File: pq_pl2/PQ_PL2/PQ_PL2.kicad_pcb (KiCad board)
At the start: 2 copper layers, 40 x 40 mm, 66 parts, among them J1 SLW-110-01-T-S, J2 SLW-110-01-T-S, J3 SLW-110-01-T-S, J4 SLW-110-01-T-S

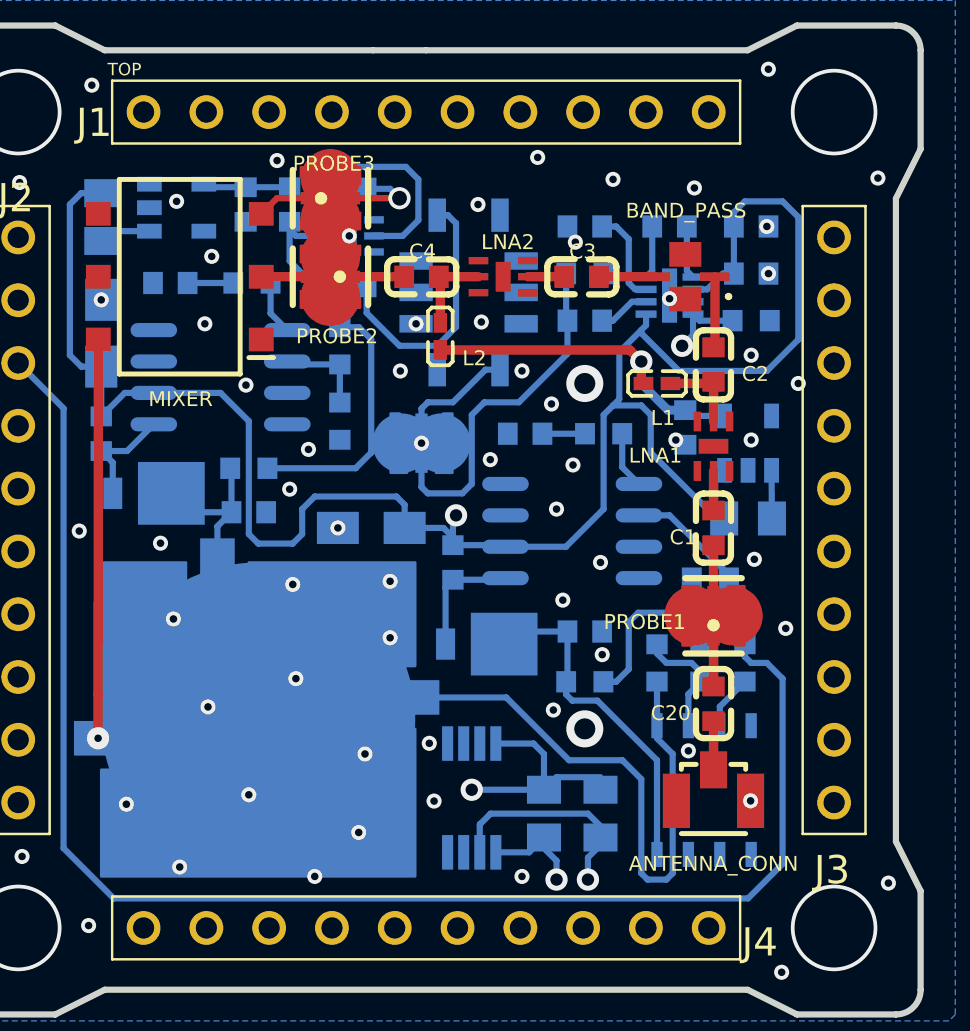
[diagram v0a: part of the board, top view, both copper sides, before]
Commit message: Solved old design components&library altium import problems. Pre KiCad7
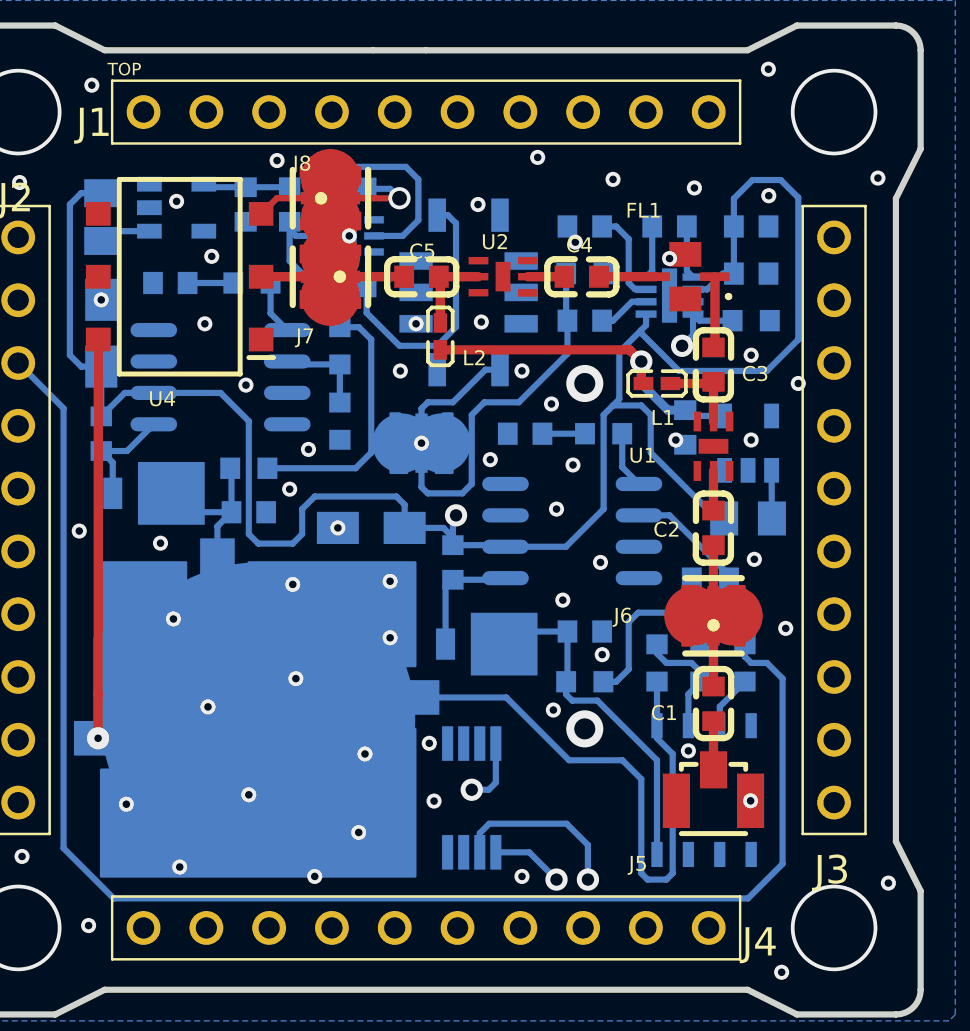
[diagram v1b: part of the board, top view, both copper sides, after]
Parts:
- removed R13, R14: 5k, easyeda:R0805
- renumbered C20 to C1, C13 to C10, C14 to C11, C15 to C12, C11 to C13, C7 to C14, C9 to C15, C12 to C16, C8 to C17, C10 to C18, C1 to C2, C18 to C20, C2 to C3, C3 to C4, C4 to C5, C5 to C6, C6 to C7, C17 to C8, C16 to C9, BAND_PASS to FL1, SAW to FL2, VCO to G1, ANTENNA_CONN to J5, PROBE1 to J6, PROBE2 to J7, PROBE3 to J8, PROBE4 to J9, R8 to R1, R3 to R10, R4 to R11, R2 to R12, R9 to R2, R10 to R3, R12 to R4, R11 to R5, R5 to R6, R6 to R7, R7 to R8, R1 to R9, LNA1 to U1, B3.6VRF to U10, B3.6VIF to U11, TSENS to U12, LNA2 to U2, OPAMP to U3, MIXER to U4, LNA3 to U5, B10V to U8, B22V to U9
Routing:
- net (no net): track 559.7 -> 552.0 mm, vias 78 -> 77
- added copper zone on In1.Cu, net (none)
- added copper zone on In2.Cu, net (none)
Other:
- copper layers 2 -> 4

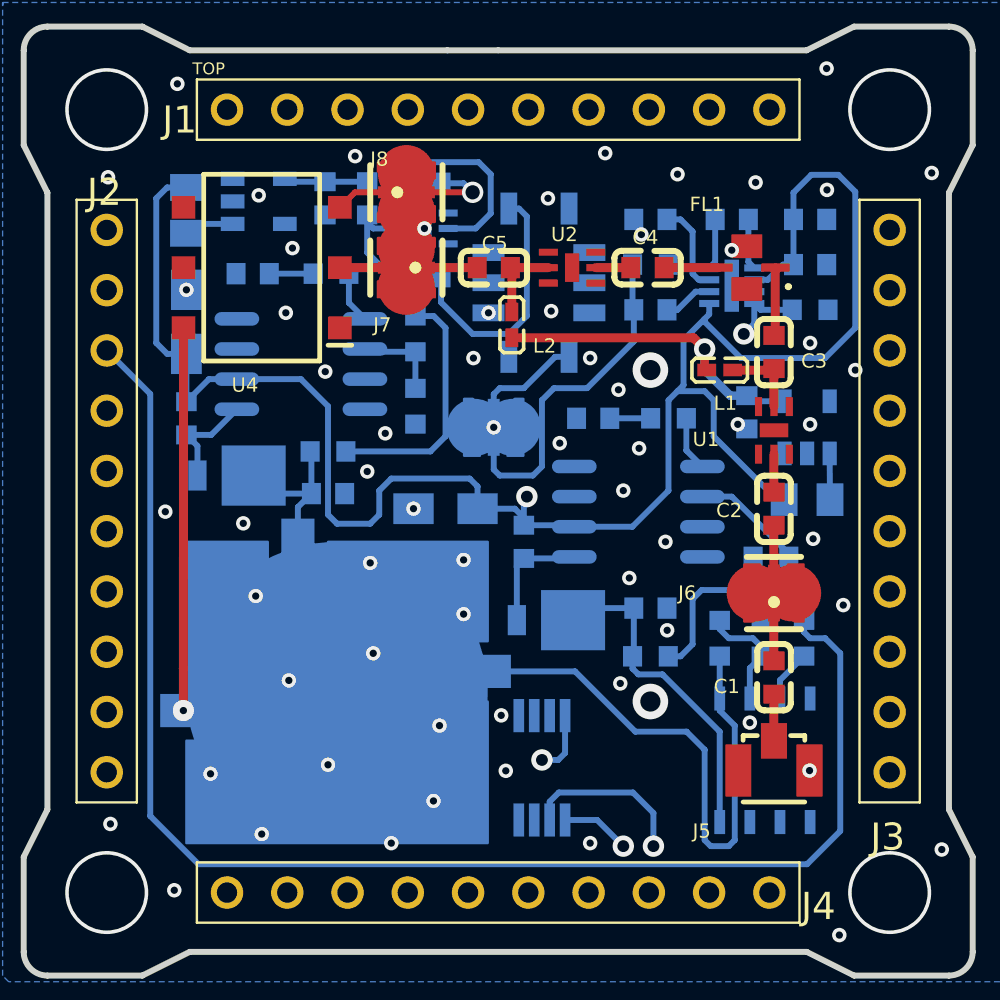
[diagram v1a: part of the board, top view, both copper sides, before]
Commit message: Full Kicad7 transition, library improvement and adaptation, correct footprints and 3D models added
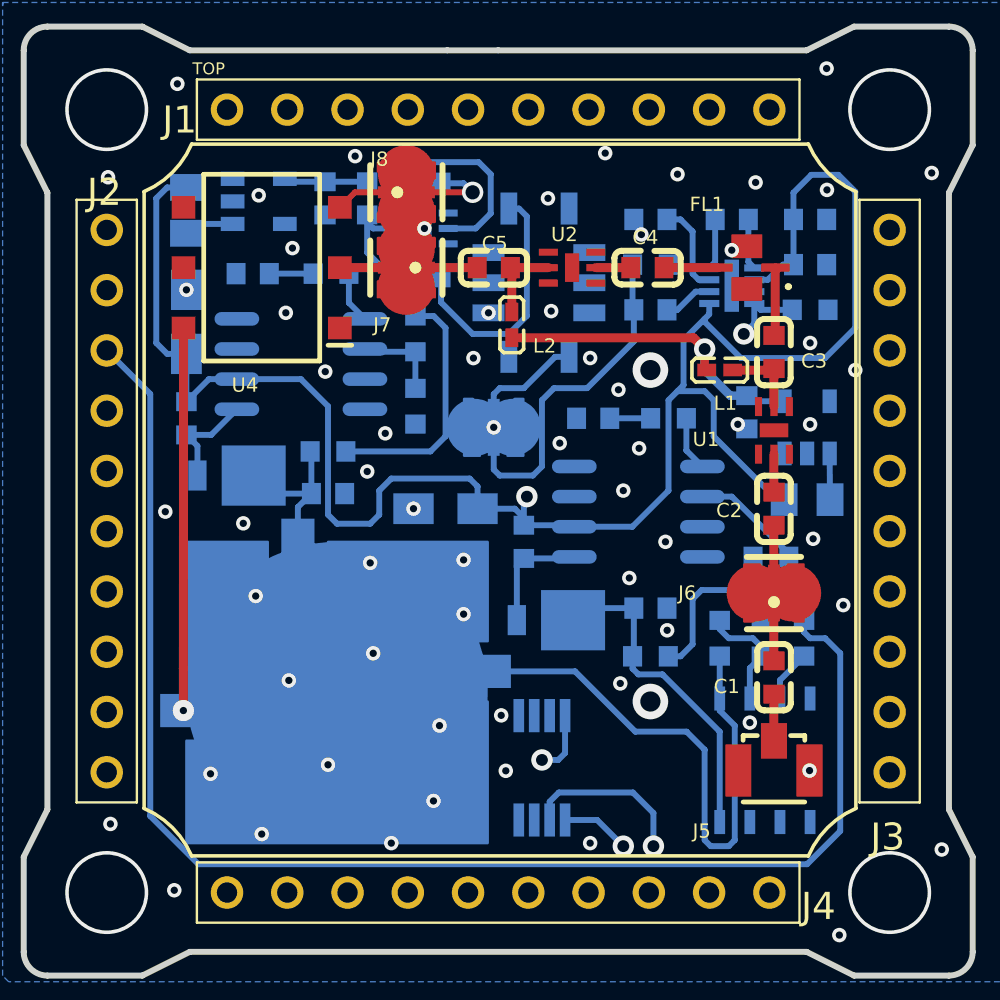
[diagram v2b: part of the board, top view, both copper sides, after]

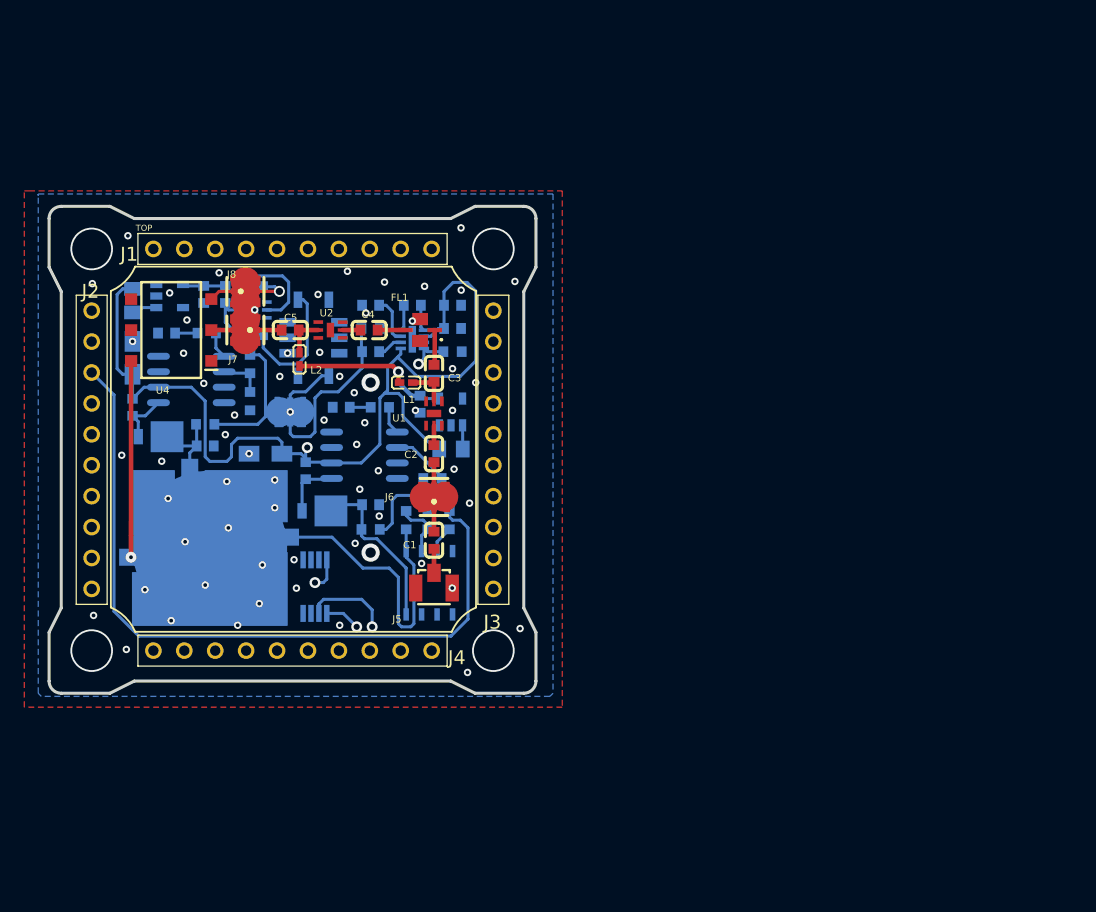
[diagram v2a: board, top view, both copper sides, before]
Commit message: P/L2 schematic revision and preliminary layout formulation: tranmission lines and block biasing
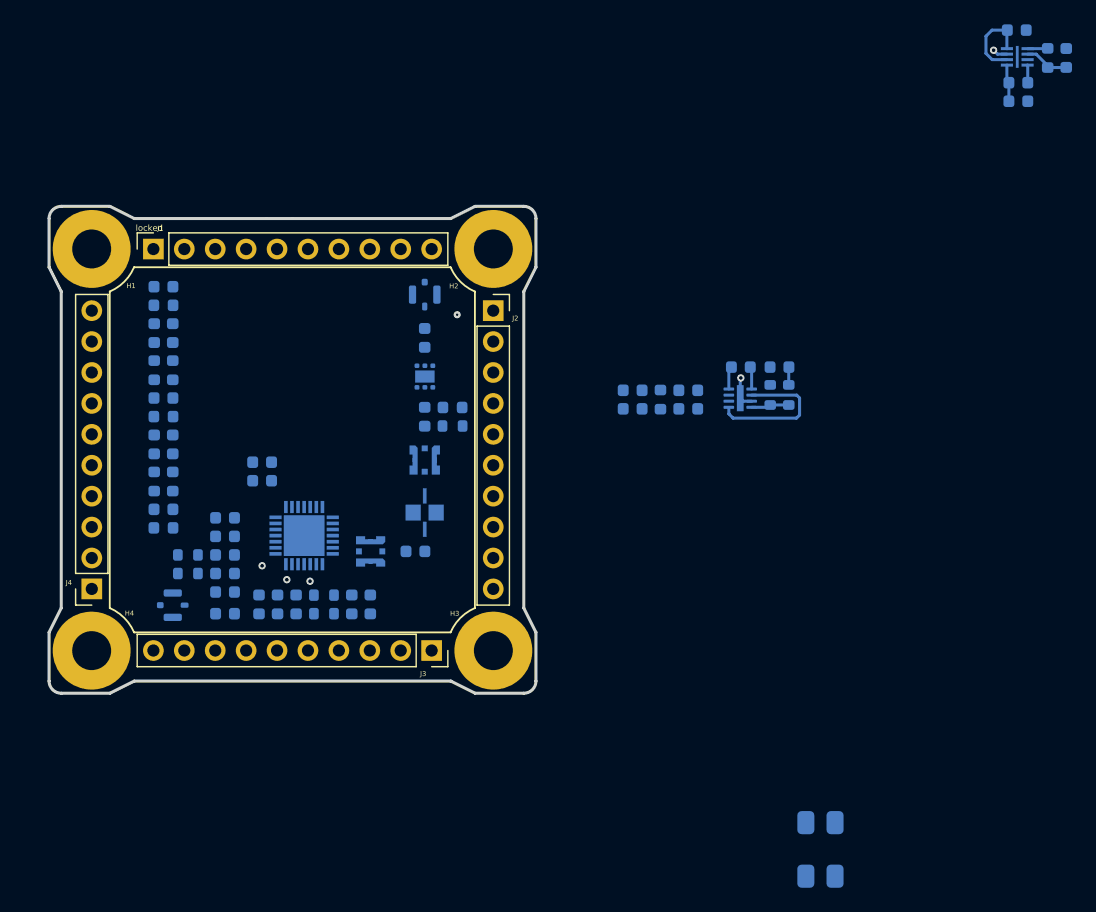
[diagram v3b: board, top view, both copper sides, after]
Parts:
- removed D1, D2: MBRM120ET3G, easyeda:POWERMITE_L2.0-W1.9-LS3.8-RD
- removed FL2: SF2242B, easyeda:SMP-03-10 5X7 MM
- removed G1: CVCO55CW, easyeda:CVCO55CW
- removed J9: MS-156C3, easyeda:IPEX-SMD_MS-156C3
- removed R10: 160K, easyeda:R0603
- removed R11: 10K, easyeda:R0603
- removed R12, R9: 68K, easyeda:R0603
- removed R8: 20K, easyeda:R0603
- removed RSSI: LT5537EDDB#TRMPBF, easyeda:SON50P200X300X80-9N
- removed U10, U11: TPS613226ADBVT, easyeda:SOT-23-5_L2.9-W1.6-P0.95-LS2.8-BR
- removed U12: TCN75AVUA713-VAO, easyeda:SOP65P490X110-8N
- removed U5: LEE2-6+, easyeda:SON65P200X200X105-7N
- removed U8, U9: LT1949ES8#PBF, easyeda:SO-8_L4.9-W3.9-P1.27-LS5.9-BL
- added Annotation1: Silkscreen_Annotation, -nsl_symbols:Bridgemaker, B.Cu at (166.8, 36.0)
- added Annotation2: Silkscreen_Annotation, -nsl_symbols:GRSS, B.Cu at (175.5, 30.8)
- added C21: 1.3pF, Capacitor_SMD:C_0603_1608Metric, B.Cu at (93.2, 58.7)
- added C22: 1.3pF, Capacitor_SMD:C_0603_1608Metric, B.Cu at (91.7, 58.7)
- added C23: 310pF, Capacitor_SMD:C_0603_1608Metric, B.Cu at (92.5, 64.0)
- added C24: 12 pF, Capacitor_SMD:C_0603_1608Metric, B.Cu at (131.0, 55.8)
- added C25: 12 pF, Capacitor_SMD:C_0603_1608Metric, B.Cu at (131.0, 54.2)
- added C26: 10nF, Capacitor_SMD:C_0603_1608Metric, B.Cu at (135.6, 55.8)
- added C27: 10nF, Capacitor_SMD:C_0603_1608Metric, B.Cu at (135.6, 54.2)
- added C28: 27pF, Capacitor_SMD:C_0603_1608Metric, B.Cu at (143.1, 52.3)
- added C29: 33nF, Capacitor_SMD:C_0603_1608Metric, B.Cu at (139.9, 52.3)
- added C30: 1uF, Capacitor_SMD:C_0603_1608Metric, B.Cu at (166.6, 26.9)
- added C31: 4.7uF, Capacitor_SMD:C_0603_1608Metric, B.Cu at (162.6, 24.6)
- added C32: 1nF, Capacitor_SMD:C_0603_1608Metric, B.Cu at (162.7, 29.0)
- added C33: 1uF, Capacitor_SMD:C_0603_1608Metric, B.Cu at (162.7, 30.5)
- added H1: MountingHole_Pad, MountingHole:MountingHole_3.2mm_M3_Pad, F.Cu at (86.6, 42.6)
- added H2: MountingHole_Pad, MountingHole:MountingHole_3.2mm_M3_Pad, F.Cu at (119.6, 42.6)
- added H3: MountingHole_Pad, MountingHole:MountingHole_3.2mm_M3_Pad, F.Cu at (119.6, 75.6)
- added H4: MountingHole_Pad, MountingHole:MountingHole_3.2mm_M3_Pad, F.Cu at (86.6, 75.6)
- added L10: 4.7uH, Inductor_SMD:L_0603_1608Metric, B.Cu at (165.1, 26.9)
- added L8: 16.4nH, Inductor_SMD:L_0603_1608Metric, B.Cu at (92.5, 65.5)
- added L9: 680 nH, Inductor_SMD:L_0603_1608Metric, B.Cu at (133.3, 55.0)
- added X1: 406C35B14M, -nsl_miscellaneous:406C35B14M, B.Cu at (146.4, 91.9)
- C1: value 33nF -> 1nF; footprint easyeda:C0603 -> Capacitor_SMD:C_0603_1608Metric; moved to B.Cu
- C10: value 1nF -> 47nF; footprint easyeda:C0603 -> Capacitor_SMD:C_0603_1608Metric; moved to B.Cu
- C11: value 1uF -> 82pF; footprint easyeda:C0603 -> Capacitor_SMD:C_0603_1608Metric; moved to B.Cu
- C12: value 33nF -> 10nF; footprint easyeda:C0603 -> Capacitor_SMD:C_0603_1608Metric; moved to B.Cu
- C13, C16: value 10uF -> 1.2nF; footprint easyeda:C0603 -> Capacitor_SMD:C_0603_1608Metric; moved to B.Cu
- C14: value 330pF -> 47nF; footprint easyeda:C0603 -> Capacitor_SMD:C_0603_1608Metric; moved to B.Cu
- C15: value 22u -> 1.2nF; footprint easyeda:CAPPM3216X180N -> Capacitor_SMD:C_0603_1608Metric; moved to B.Cu
- C17: value 330pF -> 310pF; footprint easyeda:C0603 -> Capacitor_SMD:C_0603_1608Metric; moved to B.Cu
- C18: value 22u -> 1.3pF; footprint easyeda:CAPPM3216X180N -> Capacitor_SMD:C_0603_1608Metric; moved to B.Cu
- C19: value 22uF -> 1.3pF; footprint easyeda:C0603 -> Capacitor_SMD:C_0603_1608Metric; moved to B.Cu
- C2, C3, C4: value 10pF -> 1nF; footprint easyeda:C0603 -> Capacitor_SMD:C_0603_1608Metric; moved to B.Cu
- C20: value 22uF -> 500pF; footprint easyeda:C0603 -> Capacitor_SMD:C_0603_1608Metric; moved to B.Cu
- C5: value 10pF -> 47nF; footprint easyeda:C0603 -> Capacitor_SMD:C_0603_1608Metric; moved to B.Cu
- C6, C7, C8, C9: value 100pF -> 47nF; footprint easyeda:C0603 -> Capacitor_SMD:C_0603_1608Metric; moved to B.Cu
- FL1: value BFCG-162W+ -> BFCG162W; footprint easyeda:BFCG162W -> -nsl_rf:GE0805C-3; moved to B.Cu
- J1, J2, J3, J4: footprint easyeda:SLW-110-01-X-S -> -nsl_connector:SLW-110-01
- J5: value U.FL-R-SMT-1(10) -> U.FL-R-SMT; footprint easyeda:ANT-SMD_UFL-R-SMT-1-10 -> -nsl_connector:C.FL-R-SMT-1(90); moved to B.Cu
- J6, J7: footprint easyeda:IPEX-SMD_MS-156C3 -> -nsl_connector:CoaxialSwitch_Hirose_MS-156C3_Horizontal; moved to B.Cu
- J8: value MS-156C3 -> U.FL-R-SMT; footprint easyeda:IPEX-SMD_MS-156C3 -> -nsl_connector:C.FL-R-SMT-1(90); moved to B.Cu
- L1: footprint easyeda:L0402 -> Inductor_SMD:L_0603_1608Metric; moved to B.Cu
- L2: value 100nH -> 16.4nH; footprint easyeda:L0402 -> Inductor_SMD:L_0603_1608Metric; moved to B.Cu
- L3: value 3.3uH -> 3.9nH; footprint easyeda:L0603 -> Inductor_SMD:L_0603_1608Metric; moved to B.Cu
- L4: value 10uH -> 3.9nH; footprint easyeda:L0603 -> Inductor_SMD:L_0603_1608Metric; moved to B.Cu
- L5: value 10uH -> 10.2nH; footprint easyeda:L0603 -> Inductor_SMD:L_0603_1608Metric; moved to B.Cu
- L6, L7: value 4.7uH -> 3.9nH; footprint easyeda:L0805 -> Inductor_SMD:L_0603_1608Metric; moved to B.Cu
- R1: value 10K -> 87.5; footprint easyeda:R0603 -> Resistor_SMD:R_0603_1608Metric; moved to B.Cu
- R2: value 20K -> 75; footprint easyeda:R0603 -> Resistor_SMD:R_0603_1608Metric; moved to B.Cu
- R3: value 100K -> 75; footprint easyeda:R0603 -> Resistor_SMD:R_0603_1608Metric; moved to B.Cu
- R4: value 51 -> 18k; footprint easyeda:R0603 -> Resistor_SMD:R_0603_1608Metric; moved to B.Cu
- R5: value 33K -> 2.2k; footprint easyeda:R0603 -> Resistor_SMD:R_0603_1608Metric; moved to B.Cu
- R6: value 120K -> 33K; footprint easyeda:R0603 -> Resistor_SMD:R_0603_1608Metric; moved to B.Cu
- R7: value 20K -> 33K; footprint easyeda:R0603 -> Resistor_SMD:R_0603_1608Metric; moved to B.Cu
- U1: footprint easyeda:SON65P200X200X105-7N -> Package_SON:WSON-6-1EP_2x2mm_P0.65mm_EP1x1.6mm; moved to B.Cu
- U2: value LEE2-6+ -> MAX2121; footprint easyeda:SON65P200X200X105-7N -> -nsl_rf:QFN50P500X500X80-29N; moved to B.Cu
- U3: value LM258WDT -> LT5537EDDB; footprint easyeda:SO8 -> Package_DFN_QFN:DFN-8-1EP_2x3mm_P0.5mm_EP0.56x2.15mm; moved to B.Cu
- U4: value ADE-11X+ -> LT3048; footprint easyeda:SOTFL254P691X284-6N -> -nsl_power:SON45P200X200X80-9N; moved to B.Cu
- moved U4 73.0 mm to (162.6, 26.8)
- moved R6 46.5 mm to (142.3, 54.6), turned to -90 degrees
- moved R7 44.3 mm to (143.8, 54.6)
- moved J2 33.0 mm to (119.6, 47.7), turned to 0 degrees
- moved U3 31.0 mm to (139.8, 54.9), turned to 0 degrees
- moved J3 28.4 mm to (114.5, 75.6)
- moved C14 27.9 mm to (109.5, 71.8), turned to -90 degrees
- moved C10 27.5 mm to (97.5, 69.3), turned to 0 degrees
- moved J8 26.5 mm to (93.2, 71.9), turned to -90 degrees
- moved C12 26.4 mm to (103.4, 71.8), turned to -90 degrees
- moved C4 26.1 mm to (97.5, 72.6)
- moved C11 25.9 mm to (107.9, 71.8), turned to -90 degrees
- moved L7 24.5 mm to (91.7, 61.7), turned to 90 degrees
- moved R5 24.0 mm to (105.6, 72.6), turned to 0 degrees
- moved C9 23.7 mm to (97.5, 67.8)
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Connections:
- C1 pad 1: (no net) -> Net-(C1-Pad1)
- C1 pad 2: (no net) -> Net-(U1-In)
- C10 pad 1: (no net) -> Net-(C10-Pad1)
- C10 pad 2: (no net) -> Net-(U2-QOUT+)
- C11 pad 1: (no net) -> Net-(U2-TUNEVCO)
- C11 pad 2: (no net) -> GND
- C12 pad 1: (no net) -> Net-(U2-CPOUT)
- C12 pad 2: (no net) -> Net-(C12-Pad2)
- C13 pad 1: (no net) -> Net-(U2-CPOUT)
- C13 pad 2: (no net) -> GND
- C14 pad 1: (no net) -> Net-(U2-BYPVCO)
- C14 pad 2: (no net) -> GND
- C15 pad 1: (no net) -> Net-(U2-XTAL)
- C15 pad 2: (no net) -> Net-(C15-Pad2)
- C16 pad 1: (no net) -> Net-(U2-REFOUT)
- C16 pad 2: (no net) -> Net-(C16-Pad2)
- C17 pad 1: (no net) -> IF-
- C17 pad 2: (no net) -> IF+
- C18 pad 1: (no net) -> Net-(C18-Pad1)
- C18 pad 2: (no net) -> IF+
- C19 pad 1: (no net) -> Net-(C19-Pad1)
- C19 pad 2: (no net) -> IF-
- C2 pad 1: (no net) -> Net-(U1-Out&DCin)
- C2 pad 2: (no net) -> Net-(C2-Pad2)
- C20 pad 1: (no net) -> Net-(C20-Pad1)
- C20 pad 2: (no net) -> Net-(C20-Pad2)
- C3 pad 1: (no net) -> Net-(FL1-Out)
- C3 pad 2: (no net) -> RF
- C4 pad 1: (no net) -> P/L_POWER
- C4 pad 2: (no net) -> GND
- C5 pad 1: (no net) -> Net-(U2-QDC+)
- C5 pad 2: (no net) -> Net-(U2-QDC-)
- C6 pad 1: (no net) -> Net-(U2-IDC+)
- C6 pad 2: (no net) -> Net-(U2-IDC-)
- C7 pad 1: (no net) -> IF-
- C7 pad 2: (no net) -> IO-
- C8 pad 1: (no net) -> IF+
- C8 pad 2: (no net) -> IO+
- C9 pad 1: (no net) -> Net-(C9-Pad1)
- C9 pad 2: (no net) -> Net-(U2-QOUT-)
- FL1 pad 1: (no net) -> Net-(FL1-IN)
- FL1 pad 2: (no net) -> GND
- FL1 pad 3: (no net) -> Net-(FL1-Out)
- FL1 pad 4: (no net) -> GND
- J1 pad 1: (no net) -> SDA1
- J1 pad 10: (no net) -> 3V3_PERM
- J1 pad 2: (no net) -> SCL1
- J1 pad 3: (no net) -> UART_RX
- J1 pad 4: (no net) -> KILLSWITCH+
- J1 pad 5: (no net) -> PFO
- J1 pad 6: (no net) -> BATT-
- J1 pad 7: (no net) -> NC
- J1 pad 8: (no net) -> UART_TX
- J1 pad 9: (no net) -> GND
- J2 pad 1: (no net) -> STM32_PA15
- J2 pad 10: (no net) -> GND
- J2 pad 2: (no net) -> STM32_PB3
- J2 pad 3: (no net) -> BATT_NTC
- J2 pad 4: (no net) -> SOLAR_Y
- J2 pad 5: (no net) -> SEL_PH2
- J2 pad 6: (no net) -> SEL_PH1
- J2 pad 7: (no net) -> GND
- J2 pad 8: (no net) -> HEATER_PWR
- J2 pad 9: (no net) -> BURNCOMMS
- J3 pad 1: (no net) -> SOLAR_Z
- J3 pad 10: (no net) -> CHRG
- J3 pad 2: (no net) -> STM32_PB0
- J3 pad 3: (no net) -> ADCS_POWER
- J3 pad 4: (no net) -> RST_DRIVERS
- J3 pad 5: (no net) -> ADC_PH
- J3 pad 6: (no net) -> P/L_POWER
- J3 pad 7: (no net) -> SEL_PH0
- J3 pad 8: (no net) -> VCC_UMBILICAL
- J3 pad 9: (no net) -> FAULT
- J4 pad 1: (no net) -> SOLAR_X
- J4 pad 10: (no net) -> SCL3
- J4 pad 2: (no net) -> CHGOFF
- J4 pad 3: (no net) -> CLPROG
- J4 pad 4: (no net) -> SDA3
- J4 pad 5: (no net) -> NRST
- J4 pad 6: (no net) -> SWDIO
- J4 pad 7: (no net) -> SWCLK
- J4 pad 8: (no net) -> DAC_PL
- J4 pad 9: (no net) -> ADC_PL
- J5 pad 1: (no net) -> Net-(C1-Pad1)
- J5 pad 2: (no net) -> GND
- J8 pad 1: (no net) -> Net-(C16-Pad2)
- J8 pad 2: (no net) -> GND
- L1 pad 1: (no net) -> Net-(L1-Pad1)
- L1 pad 2: (no net) -> Net-(U1-Out&DCin)
- L2 pad 1: (no net) -> IF+
- L2 pad 2: (no net) -> IF-
- L3 pad 1: (no net) -> Net-(C20-Pad2)
- L3 pad 2: (no net) -> Net-(C18-Pad1)
- L4 pad 1: (no net) -> Net-(C20-Pad1)
- L4 pad 2: (no net) -> Net-(C19-Pad1)
- L5 pad 1: (no net) -> Net-(C20-Pad2)
- L5 pad 2: (no net) -> Net-(C20-Pad1)
- L6 pad 1: (no net) -> RSSI+
- L6 pad 2: (no net) -> Net-(C21-Pad1)
- L7 pad 1: (no net) -> RSSI-
- L7 pad 2: (no net) -> Net-(C22-Pad1)
- R1 pad 1: (no net) -> 5V
- R1 pad 2: (no net) -> Net-(L1-Pad1)
- R2 pad 1: (no net) -> Net-(C9-Pad1)
- R2 pad 2: (no net) -> GND
- R3 pad 1: (no net) -> Net-(C10-Pad1)
- R3 pad 2: (no net) -> GND
- R4 pad 1: (no net) -> Net-(U2-TUNEVCO)
- R4 pad 2: (no net) -> Net-(U2-CPOUT)
- R5 pad 1: (no net) -> Net-(C12-Pad2)
- R5 pad 2: (no net) -> GND
- R6 pad 1: (no net) -> GND
- R6 pad 2: (no net) -> Net-(U3-OUT)
- R7 pad 1: (no net) -> Net-(U3-OUT)
- R7 pad 2: (no net) -> ADC_PL
- U1 pad 1: (no net) -> GND
- U1 pad 2: (no net) -> Net-(U1-In)
- U1 pad 3: (no net) -> GND
- U1 pad 4: (no net) -> GND
- U1 pad 5: (no net) -> Net-(U1-Out&DCin)
- U1 pad 6: (no net) -> GND
- U1 pad 7: (no net) -> GND
- U2 pad 1: (no net) -> P/L_POWER
- U2 pad 2: (no net) -> P/L_POWER
- U2 pad 3: (no net) -> GND
- U2 pad 4: (no net) -> Net-(U2-RFIN)
- U2 pad 5: (no net) -> DAC_PL
- U2 pad 6: (no net) -> P/L_POWER
- U2 pad 7: (no net) -> P/L_POWER
- U3 pad 1: (no net) -> P/L_POWER
- U3 pad 2: (no net) -> Net-(U3-IN+)
- U3 pad 3: (no net) -> Net-(U3-IN-)
- U3 pad 4: (no net) -> Net-(U3-CAP+)
- U3 pad 5: (no net) -> Net-(U3-CAP-)
- U3 pad 6: (no net) -> P/L_POWER
- U3 pad 7: (no net) -> GND
- U3 pad 8: (no net) -> Net-(U3-OUT)
- U4 pad 1: (no net) -> Net-(U4-SW)
- U4 pad 2: (no net) -> P/L_POWER
- U4 pad 3: (no net) -> GND
- U4 pad 4: (no net) -> Net-(U4-BYP)
- U4 pad 5: (no net) -> 5V
- U4 pad 6: (no net) -> Net-(U4-BSOUT)
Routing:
- net (no net): track 552.0 -> 0.00 mm, vias 77 -> 0
- net P/L_POWER: track 0.00 -> 17.0 mm, vias 0 -> 3
- net Net-(U4-BSOUT): track 0.00 -> 6.85 mm
- net Net-(U3-OUT): track 0.00 -> 3.13 mm
- net 5V: track 0.00 -> 3.04 mm
- net GND: track 0.00 -> 2.72 mm, vias 0 -> 2
- net Net-(U3-CAP+): track 0.00 -> 1.89 mm
- net Net-(U3-CAP-): track 0.00 -> 1.85 mm
- net Net-(U4-SW): track 0.00 -> 1.66 mm
- net ADC_PL: track 0.00 -> 1.47 mm
- net Net-(U4-BYP): track 0.00 -> 1.45 mm
- net Net-(C1-Pad1): vias 0 -> 1
- removed copper zone on B.Cu, net (none)
- removed copper zone on F.Cu, net (none)
- removed copper zone on In1.Cu, net (none)
- removed copper zone on In2.Cu, net (none)
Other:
- board text added: "locked"
- board text removed: "BOTTOM"
- board text removed: "TOP"
